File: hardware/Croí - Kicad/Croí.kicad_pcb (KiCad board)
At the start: 4 copper layers, 60 x 60 mm, 46 parts, among them J1 JTAG-10 PIN, J2 XT30PW-M, J3 ESQ-110-14-G-D, Q1 IPP060N06N, U1 W25Q128JVS, U2 ADXL375BCCZ, U3 STM32F072C8Tx, U4 BME680, U5 BMP390, U7 TLV70433DBVT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

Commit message: major changes
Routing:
- net GND: track 30.4 -> 43.3 mm
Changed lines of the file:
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@@
+	)
+	(segment
+		(start 38.9563 39.2937)
+		(end 38.9563 40.310301)
+		(width 0.2)
+		(layer "F.Cu")
+		(net 1)
 	)
 	(segment
@@
 	)
 	(segment
+		(start 39.026008 39.223992)
+		(end 38.9563 39.2937)
+		(width 0.2)
+		(layer "F.Cu")
+		(net 1)
+	)
+	(segment
 		(start 53.73 53)
 		(end 54.5 53)
@@
 		(start 38.400057 52)
 		(end 37.175 52)
-		(width 0.2)
-		(layer "F.Cu")
-		(net 1)
-	)
-	(segment
-		(start 38.9563 40.310301)
-		(end 38.9563 39.2937)
 		(width 0.2)
 		(layer "F.Cu")
@@
 	)
 	(segment
+		(start 39.026008 39.003429)
+		(end 39.026008 39.223992)
+		(width 0.2)
+		(layer "F.Cu")
+		(net 1)
+	)
+	(segment
 		(start 37.7063 40.960301)
 		(end 37.357203 40.611204)
@@
 	)
 	(segment
-		(start 38.9563 39.2937)
-		(end 39.25 39)
-		(width 0.2)
-		(layer "F.Cu")
-		(net 1)
-	)
-	(segment
 		(start 39.15 52.25)
 		(end 38.650057 52.25)
@@
 	)
 	(via
-		(at 39.25 39)
+		(at 39.026008 39.003429)
 		(size 0.6)
 		(drill 0.3)
@@
 	)
 	(segment
+		(start 39.253429 39.003429)
+		(end 39.026008 39.003429)
+		(width 0.6)
+		(layer "In2.Cu")
+		(net 1)
+	)
+	(segment
 		(start 49.156085 44.977299)
 		(end 55.5 51.321214)
@@
 	)
 	(segment
-		(start 38.25 38)
-		(end 39.25 39)
-		(width 0.6)
-		(layer "In2.Cu")
-		(net 1)
-	)
-	(segment
 		(start 40.471635 46.25)
 		(end 40.471635 43.671675)
@@
 	)
 	(segment
+		(start 39.026008 39.003429)
+		(end 39.026008 38.776008)
+		(width 0.6)
+		(layer "In2.Cu")
+		(net 1)
+	)
+	(segment
+		(start 39.026008 38.776008)
+		(end 38.25 38)
+		(width 0.6)
+		(layer "In2.Cu")
+		(net 1)
+	)
+	(segment
 		(start 39.551 51.168214)
 		(end 40.471635 50.247579)
@@
 	)
 	(segment
-		(start 38.25 33.5)
-		(end 38.25 38)
-		(width 0.6)
-		(layer "In2.Cu")
-		(net 1)
-	)
-	(segment
 		(start 38.75 33)
 		(end 42.75 33)
@@
 		(start 40.04996 39.79996)
 		(end 39.625 39.375)
+		(width 0.6)
+		(layer "In2.Cu")
+		(net 1)
+	)
+	(segment
+		(start 39.625 39.375)
+		(end 39.253429 39.003429)
 		(width 0.6)
 		(layer "In2.Cu")
@@
 	)
 	(segment
+		(start 38.25 38)
+		(end 38.25 33.5)
+		(width 0.6)
+		(layer "In2.Cu")
+		(net 1)
+	)
+	(segment
 		(start 44.54 64.5)
 		(end 44.54 67.04)
@@
 	)
 	(segment
-		(start 39.625 39.375)
-		(end 39.25 39)
-		(width 0.6)
-		(layer "In2.Cu")
-		(net 1)
-	)
-	(segment
 		(start 32 27.5)
 		(end 32.25 27.5)
@@
 	)
 	(segment
+		(start 39.627008 40.872992)
+		(end 38.9563 41.5437)
+		(width 0.2)
+		(layer "F.Cu")
+		(net 2)
+	)
+	(segment
 		(start 44.2874 37.212599)
 		(end 44.2874 36.7126)
@@
 	)
 	(segment
+		(start 37.729533 37.549591)
+		(end 37.7063 37.526358)
+		(width 0.2)
+		(layer "F.Cu")
+		(net 2)
+	)
+	(segment
+		(start 41.776907 36.12315)
+		(end 40.75 37.150057)
+		(width 0.2)
+		(layer "F.Cu")
+		(net 2)
+	)
+	(segment
+		(start 38.83366 37.399)
+		(end 38.683069 37.549591)
+		(width 0.2)
+		(layer "F.Cu")
+		(net 2)
+	)
+	(segment
 		(start 43.9 43.862192)
 		(end 43.858907 43.903285)
@@
 	)
 	(segment
+		(start 37.2063 36.960301)
+		(end 37.7063 36.960301)
+		(width 0.2)
+		(layer "F.Cu")
+		(net 2)
+	)
+	(segment
 		(start 45.205543 36.7126)
 		(end 45.496878 37.003935)
@@
 	)
 	(segment
+		(start 37.7063 37.526358)
+		(end 37.2063 37.026358)
+		(width 0.2)
+		(layer "F.Cu")
+		(net 2)
+	)
+	(segment
 		(start 60 49.75)
 		(end 59.26 49.75)
@@
 	)
 	(segment
+		(start 37.2063 37.026358)
+		(end 37.2063 36.960301)
+		(width 0.2)
+		(layer "F.Cu")
+		(net 2)
+	)
+	(segment
+		(start 41.850759 36.12315)
+		(end 41.776907 36.12315)
+		(width 0.2)
+		(layer "F.Cu")
+		(net 2)
+	)
+	(segment
 		(start 39.0875 45.3925)
 		(end 39.48 45)
@@
 	)
 	(segment
+		(start 39.627008 38.754486)
+		(end 39.627008 40.872992)
+		(width 0.2)
+		(layer "F.Cu")
+		(net 2)
+	)
+	(segment
+		(start 38.246008 39.101667)
+		(end 38.246008 38.791668)
+		(width 0.2)
+		(layer "F.Cu")
+		(net 2)
+	)
+	(segment
+		(start 38.246008 38.791668)
+		(end 38.635247 38.402429)
+		(width 0.2)
+		(layer "F.Cu")
+		(net 2)
+	)
+	(segment
+		(start 40.501883 37.399)
+		(end 38.83366 37.399)
+		(width 0.2)
+		(layer "F.Cu")
+		(net 2)
+	)
+	(segment
+		(start 39.274951 38.402429)
+		(end 39.627008 38.754486)
+		(width 0.2)
+		(layer "F.Cu")
+		(net 2)
+	)
+	(segment
+		(start 37.7063 36.960301)
+		(end 37.7063 37.526358)
+		(width 0.2)
+		(layer "F.Cu")
+		(net 2)
+	)
+	(segment
 		(start 38.157201 39.190474)
 		(end 38.246008 39.101667)
@@
 	)
 	(segment
+		(start 38.635247 38.402429)
+		(end 39.274951 38.402429)
+		(width 0.2)
+		(layer "F.Cu")
+		(net 2)
+	)
+	(segment
 		(start 42.737146 34.237146)
 		(end 42.25 33.75)
@@
 	)
 	(segment
+		(start 40.75 37.150057)
+		(end 40.75 37.150883)
+		(width 0.2)
+		(layer "F.Cu")
+		(net 2)
+	)
+	(segment
 		(start 50.37 49.27)
 		(end 50.525 49.115)
@@
 	)
 	(segment
+		(start 38.683069 37.549591)
+		(end 37.729533 37.549591)
+		(width 0.2)
+		(layer "F.Cu")
+		(net 2)
+	)
+	(segment
 		(start 38.75 51.5)
 		(end 37.175 51.5)
@@
 		(start 42.737146 34.817675)
 		(end 42.737146 34.237146)
+		(width 0.2)
+		(layer "F.Cu")
+		(net 2)
+	)
+	(segment
+		(start 38.9563 41.5437)
+		(end 38.9563 42.710301)
+		(width 0.2)
+		(layer "F.Cu")
+		(net 2)
+	)
+	(segment
+		(start 40.75 37.150883)
+		(end 40.501883 37.399)
 		(width 0.2)
 		(layer "F.Cu")
@@
 	)
 	(segment
-		(start 40 39)
+		(start 40 39.375)
 		(end 40 38)
 		(width 0.2)
@@
 	)
 	(segment
-		(start 35.75 43.25)
-		(end 40 39)
+		(start 35.75 43.625)
+		(end 40 39.375)
 		(width 0.2)
 		(layer "B.Cu")
@@
 	(segment
 		(start 35.75 45.25)
-		(end 35.75 43.25)
+		(end 35.75 43.625)
 		(width 0.2)
 		(layer "B.Cu")
@@
 	)
 	(segment
-		(start 39.5 40.75)
-		(end 41.75 38.5)
-		(width 0.2)
-		(layer "B.Cu")
-		(net 13)
-	)
-	(segment
 		(start 38 56.5)
 		(end 40 56.5)
@@
 	)
 	(segment
-		(start 37.25 42.5)
-		(end 39 40.75)
+		(start 37.620339 44.57214)
+		(end 37.25 44.201801)
 		(width 0.2)
 		(layer "B.Cu")
@@
 	)
 	(segment
-		(start 37.620339 44.57214)
-		(end 37.25 44.201801)
-		(width 0.2)
-		(layer "B.Cu")
-		(net 13)
-	)
-	(segment
 		(start 41.75 37)
 		(end 41.75 38.5)
@@
 	)
 	(segment
-		(start 37.25 44.201801)
-		(end 37.25 42.5)
+		(start 37.25 43)
+		(end 41.75 38.5)
 		(width 0.2)
 		(layer "B.Cu")
@@
 	)
 	(segment
-		(start 39 40.75)
-		(end 39.5 40.75)
-		(width 0.2)
-		(layer "B.Cu")
+		(start 37.25 44.201801)
+		(end 37.25 43)
+		(width 0.2)
+		(layer "B.Cu")

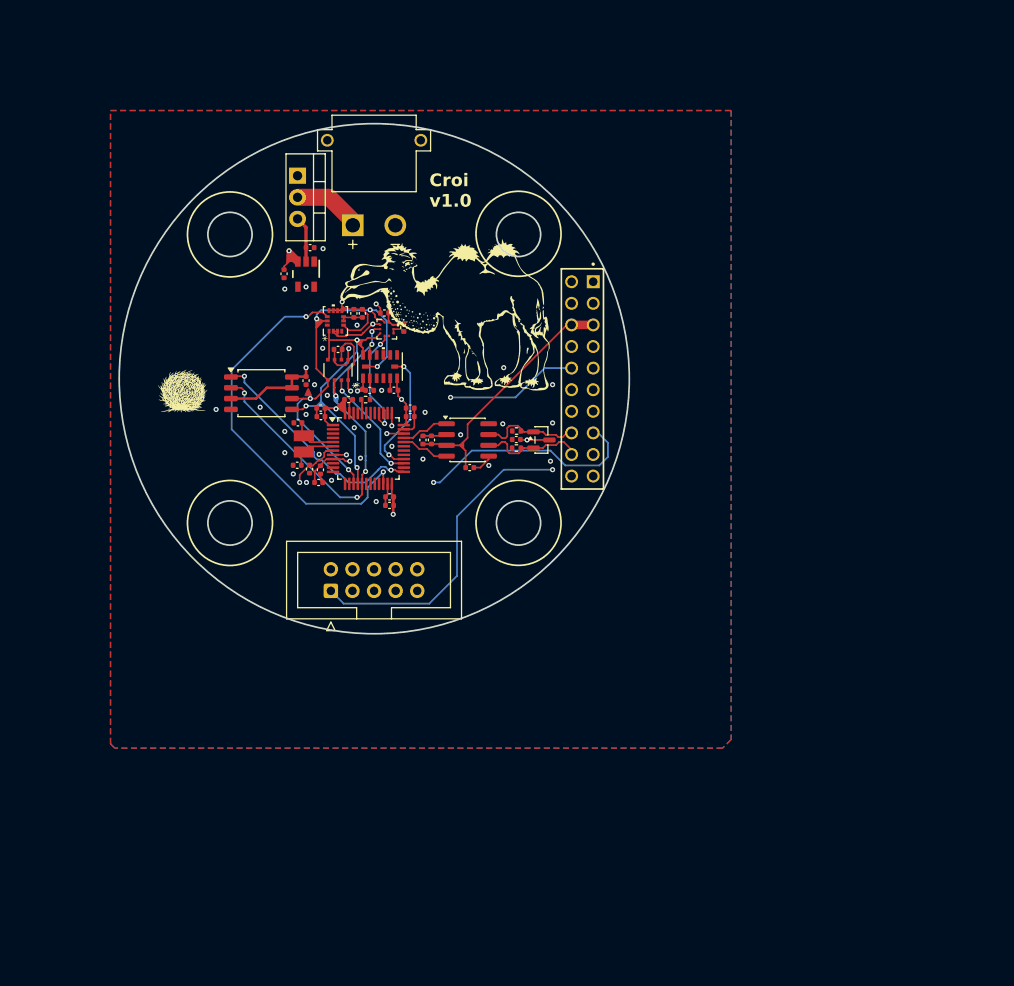
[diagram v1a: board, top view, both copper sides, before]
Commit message: repositioned board
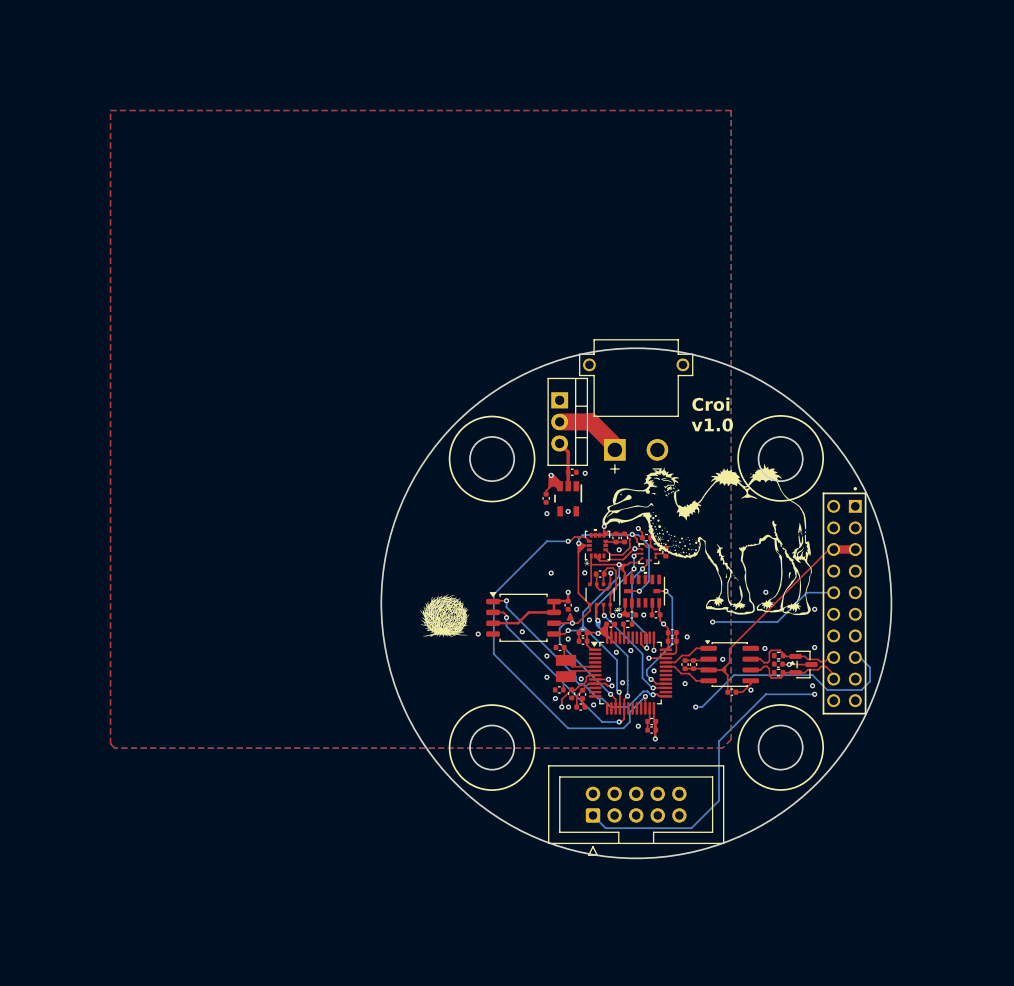
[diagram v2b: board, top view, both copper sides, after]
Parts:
- moved C3 40.6 mm to (72.3, 70.3)
- moved C10 40.6 mm to (66.3, 81.2)
- moved C2 40.6 mm to (66.6, 72.4)
- moved C23 40.6 mm to (62.2, 56.6)
- moved C26 40.6 mm to (89.6, 76.1)
- moved C11 40.6 mm to (71.5, 61.3)
- moved C12 40.6 mm to (66.5, 79.7)
- moved C15 40.6 mm to (77.1, 72.4)
- moved C17 40.6 mm to (77.1, 73.4)
- moved C18 40.6 mm to (74.0, 61.2)
- moved C19 40.6 mm to (68.6, 65.5)
- moved C21 40.6 mm to (65.3, 53.5)
- moved C22 40.6 mm to (84.1, 79.4)
- moved C24 40.6 mm to (78.6, 76.2)
- moved C25 40.6 mm to (79.6, 76.2)
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
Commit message: random ass changes
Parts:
- added J4: 436500303, footprints2:MOLEX_436500303, F.Cu at (52.5, 72.0)
- added U6: ~, Library:Untitled, F.Cu at (6.60, 8.60)

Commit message: Crazy new changes
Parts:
- moved U6 96.8 mm to (84.5, 66.0)
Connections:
- U6 pad 1: (no net) -> 3.3V
- U6 pad 2: (no net) -> GND
- U6 pad 3: (no net) -> unconnected-(U6-Vin_Passthrough-Pad3)
- U6 pad 4: (no net) -> GND
- U6 pad 5: (no net) -> Net-(U6-Video)
- U6 pad 6: (no net) -> unconnected-(U6-unimportant-Pad6)
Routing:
- net Net-(U6-Video): track 0.00 -> 38.8 mm, vias 0 -> 1
- net 3.3V: track 150.1 -> 159.5 mm, vias 11 -> 13
- net GND: vias 36 -> 37
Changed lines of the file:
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@@
 	(net 67 "unconnected-(U3-PB13-Pad26)")
 	(net 68 "Net-(U6-Video)")
+	(net 69 "unconnected-(U6-Vin_Passthrough-Pad3)")
+	(net 70 "unconnected-(U6-unimportant-Pad6)")
 	(footprint "Capacitor_SMD:C_0402_1005Metric"
 		(placed yes)
@@
 		)
 	)
+	(footprint "Library:Untitled"
+		(layer "F.Cu")
+		(at 84.5 66)
+		(property "Reference" "U6"
+			(at 0 -0.5 0)
+			(unlocked yes)
+			(layer "F.SilkS")
+			(hide yes)
+			(effects
+				(font
+					(size 1 1)
+					(thickness 0.1)
+				)
+			)
+		)
+		(property "Value" "~"
+			(at 0 1 0)
+			(unlocked yes)
+			(layer "F.Fab")
+			(hide yes)
+			(effects
+				(font
+					(size 1 1)
+					(thickness 0.15)
+				)
+			)
+		)
+		(property "Datasheet" ""
+			(at 0 0 0)
+			(unlocked yes)
+			(layer "F.Fab")
+			(hide yes)
+			(effects
+				(font
+					(size 1 1)
+					(thickness 0.15)
+				)
+			)
+		)
+		(property "Description" ""
+			(at 0 0 0)
+			(unlocked yes)
+			(layer "F.Fab")
+			(hide yes)
+			(effects
+				(font
+					(size 1 1)
+					(thickness 0.15)
+				)
+			)
+		)
+		(sheetname "/")
+		(sheetfile "Croí.kicad_sch")
+		(attr smd)
+		(fp_line
+			(start -6.5 -8.5)
+			(end -6.5 6.5)
+			(stroke
+				(width 0.2)
+				(type default)
+			)
+			(layer "F.Cu")
+		)
+		(fp_line
+			(start -6.5 6.5)
+			(end 6.5 6.5)
+			(stroke
+				(width 0.2)
+				(type default)
+			)
+			(layer "F.Cu")
+		)
+		(fp_line
+			(start 6.5 -8.5)
+			(end -6.5 -8.5)
+			(stroke
+				(width 0.2)
+				(type default)
+			)
+			(layer "F.Cu")
+		)
+		(fp_line
+			(start 6.5 6.5)
+			(end 6.5 -8.5)
+			(stroke
+				(width 0.2)
+				(type default)
+			)
+			(layer "F.Cu")
+		)
+		(pad "1" smd circle
+			(at -5 -7 90)
+			(size 0.8 0.8)
+			(layers "F.Cu" "F.Mask" "F.Paste")
+			(net 1 "3.3V")
+			(pinfunction "3.3V")
+			(pintype "bidirectional")
+		)
+		(pad "2" smd circle
+			(at -3 -7 90)
+			(size 0.8 0.8)
+			(layers "F.Cu" "F.Mask" "F.Paste")
+			(net 2 "GND")
+			(pinfunction "GND")
+			(pintype "bidirectional")
+		)
+		(pad "3" smd circle
+			(at -1 -7 90)
+			(size 0.8 0.8)
+			(layers "F.Cu" "F.Mask" "F.Paste")
+			(net 69 "unconnected-(U6-Vin_Passthrough-Pad3)")
+			(pinfunction "Vin_Passthrough")
+			(pintype "bidirectional+no_connect")
+		)
+		(pad "4" smd circle
+			(at 1 -7 90)
+			(size 0.8 0.8)
+			(layers "F.Cu" "F.Mask" "F.Paste")
+			(net 2 "GND")
+			(pinfunction "GND")
+			(pintype "bidirectional")
+		)
+		(pad "5" smd circle
+			(at 3 -7 90)
+			(size 0.8 0.8)
+			(layers "F.Cu" "F.Mask" "F.Paste")
+			(net 68 "Net-(U6-Video)")
+			(pinfunction "Video")
+			(pintype "bidirectional")
+		)
+		(pad "6" smd circle
+			(at 5 -7 90)
+			(size 0.8 0.8)
+			(layers "F.Cu" "F.Mask" "F.Paste")
+			(net 70 "unconnected-(U6-unimportant-Pad6)")
+			(pinfunction "unimportant")
+			(pintype "bidirectional+no_connect")
+		)
+		(embedded_fonts no)
+	)
 	(footprint "footprints:SAMTEC_ESQ-110-14-G-D"
 		(layer "F.Cu")
@@
 		)
 	)
-	(footprint "Library:Untitled"
-		(layer "F.Cu")
-		(at 6.6 8.6)
-		(property "Reference" "U6"
-			(at 0 -0.5 0)
-			(unlocked yes)
-			(layer "F.SilkS")
-			(hide yes)
-			(effects
-				(font
-					(size 1 1)
-					(thickness 0.1)
-				)
-			)
-		)
-		(property "Value" "~"
-			(at 0 1 0)
-			(unlocked yes)
-			(layer "F.Fab")
-			(hide yes)
-			(effects
-				(font
-					(size 1 1)
-					(thickness 0.15)
-				)
-			)
-		)
-		(property "Datasheet" ""
-			(at 0 0 0)
-			(unlocked yes)
-			(layer "F.Fab")
-			(hide yes)
-			(effects
-				(font
-					(size 1 1)
-					(thickness 0.15)
-				)
-			)
-		)
-		(property "Description" ""
-			(at 0 0 0)
-			(unlocked yes)
-			(layer "F.Fab")
-			(hide yes)
-			(effects
-				(font
-					(size 1 1)
-					(thickness 0.15)
-				)
-			)
-		)
-		(sheetname "/")
-		(sheetfile "Croí.kicad_sch")
-		(attr smd)
-		(fp_line
-			(start -6.5 -8.5)
-			(end -6.5 6.5)
-			(stroke
-				(width 0.2)
-				(type default)
-			)
-			(layer "F.Cu")
-		)
-		(fp_line
-			(start -6.5 6.5)
-			(end 6.5 6.5)
-			(stroke
-				(width 0.2)
-				(type default)
-			)
-			(layer "F.Cu")
-		)
-		(fp_line
-			(start 6.5 -8.5)
-			(end -6.5 -8.5)
-			(stroke
-				(width 0.2)
-				(type default)
-			)
-			(layer "F.Cu")
-		)
-		(fp_line
-			(start 6.5 6.5)
-			(end 6.5 -8.5)
-			(stroke
-				(width 0.2)
-				(type default)
-			)
-			(layer "F.Cu")
-		)
-		(pad "1" smd circle
-			(at -5 -7 90)
-			(size 0.8 0.8)
-			(layers "F.Cu" "F.Mask" "F.Paste")
-		)
-		(pad "2" smd circle
-			(at -3 -7 90)
-			(size 0.8 0.8)
-			(layers "F.Cu" "F.Mask" "F.Paste")
-		)
-		(pad "3" smd circle
-			(at -1 -7 90)
-			(size 0.8 0.8)
-			(layers "F.Cu" "F.Mask" "F.Paste")
-		)
-		(pad "4" smd circle
-			(at 1 -7 90)
-			(size 0.8 0.8)
-			(layers "F.Cu" "F.Mask" "F.Paste")
-		)
-		(pad "5" smd circle
-			(at 3 -7 90)
-			(size 0.8 0.8)
-			(layers "F.Cu" "F.Mask" "F.Paste")
-		)
-		(pad "6" smd circle
-			(at 5 -7 90)
-			(size 0.8 0.8)
-			(layers "F.Cu" "F.Mask" "F.Paste")
-		)
-		(embedded_fonts no)
-	)
 	(footprint "Capacitor_SMD:C_0402_1005Metric"
 		(placed yes)
@@
 	)
 	(segment
+		(start 79.5 59)
+		(end 79.5 60)
+		(width 0.2)
+		(layer "F.Cu")
+		(net 1)
+	)
+	(segment
 		(start 74.528146 61.236675)
 		(end 74.528146 60.471854)
@@
 	)
 	(segment
+		(start 77.5 60.5)
+		(end 76.327878 61.672122)
+		(width 0.2)
+		(layer "F.Cu")
+		(net 1)
+	)
+	(segment
 		(start 67.041 72.419)
 		(end 67.041 73.399)
@@
 	)
 	(segment
+		(start 76.327878 61.672122)
+		(end 76.327878 62.462935)
+		(width 0.2)
+		(layer "F.Cu")
+		(net 1)
+	)
+	(segment
 		(start 75.081 84.919)
 		(end 75.081 82.922528)
@@
 	)
 	(segment
+		(start 52.5 72)
+		(end 53.196 71.304)
+		(width 0.2)
+		(layer "F.Cu")
+		(net 1)
+	)
+	(segment
 		(start 68.26391 72.419)
 		(end 68.354996 72.510086)
@@
 	)
 	(segment
+		(start 53.196 71.304)
+		(end 55.9935 71.304)
+		(width 0.2)
+		(layer "F.Cu")
+		(net 1)
+	)
+	(segment
 		(start 69.199576 60.796426)
 		(end 69.037301 60.958701)
@@
 	)
 	(via
+		(at 79.5 60)
+		(size 0.6)
+		(drill 0.3)
+		(layers "F.Cu" "B.Cu")
+		(net 1)
+	)
+	(via
 		(at 68.354996 72.510086)
 		(size 0.6)
@@
 	)
 	(via
+		(at 77.5 60.5)
+		(size 0.6)
+		(drill 0.3)
+		(layers "F.Cu" "B.Cu")
+		(net 1)
+	)
+	(via
 		(at 69.981 78.669)
 		(size 0.6)
@@
 	)
 	(segment
+		(start 79 60.5)
+		(end 77.5 60.5)
+		(width 0.2)
+		(layer "B.Cu")
+		(net 1)
+	)
+	(segment
+		(start 79.5 60)
+		(end 79 60.5)
+		(width 0.2)
+		(layer "B.Cu")
+		(net 1)
+	)
+	(segment
 		(start 70.88096 70.410763)
 		(end 71.866496 71.396299)
@@
 	)
 	(via
+		(at 83.5 60)
+		(size 0.6)
+		(drill 0.3)
+		(layers "F.Cu" "B.Cu")
+		(free yes)
+		(net 2)
+	)
+	(via
 		(at 67.331 70.919)
 		(size 0.6)
@@
 		(net 66)
 	)
+	(segment
+		(start 87 59.5)
+		(end 87.5 59)
+		(width 0.2)
+		(layer "F.Cu")
+		(net 68)
+	)
+	(segment
+		(start 87 61)
+		(end 87 59.5)
+		(width 0.2)
+		(layer "F.Cu")
+		(net 68)
+	)
+	(via
+		(at 87 61)
+		(size 0.6)
+		(drill 0.3)
+		(layers "F.Cu" "B.Cu")
+		(net 68)
+	)
+	(segment
+		(start 52.5 66)
+		(end 55.98 62.52)
+		(width 0.2)
+		(layer "In1.Cu")
+		(net 68)
+	)
+	(segment
+		(start 70.130057 62.52)
+		(end 71.186011 61.464046)
+		(width 0.2)
+		(layer "In1.Cu")
+		(net 68)
+	)
+	(segment
+		(start 71.186011 61.464046)
+		(end 86.535954 61.464046)
+		(width 0.2)
+		(layer "In1.Cu")
+		(net 68)
+	)
+	(segment
+		(start 55.98 62.52)
+		(end 70.130057 62.52)
+		(width 0.2)
+		(layer "In1.Cu")
+		(net 68)
+	)
+	(segment
+		(start 86.535954 61.464046)
+		(end 87 61)
+		(width 0.2)
+		(layer "In1.Cu")
+		(net 68)
+	)
 	(zone
